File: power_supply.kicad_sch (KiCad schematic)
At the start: 59 parts, among them Q1201 NX7002AK, Q1202 PMN48XP, U1201 TL431AFDT, U1202 TL431AFDT, U1203 TL431AFDT, U1204 MCP1824T-330, U1205 NCV8164ASN120T1G, U1206 MCP1824T-330, U1207 NCV8164ASN250T1G, U1208 NCV8164ASN330T1G

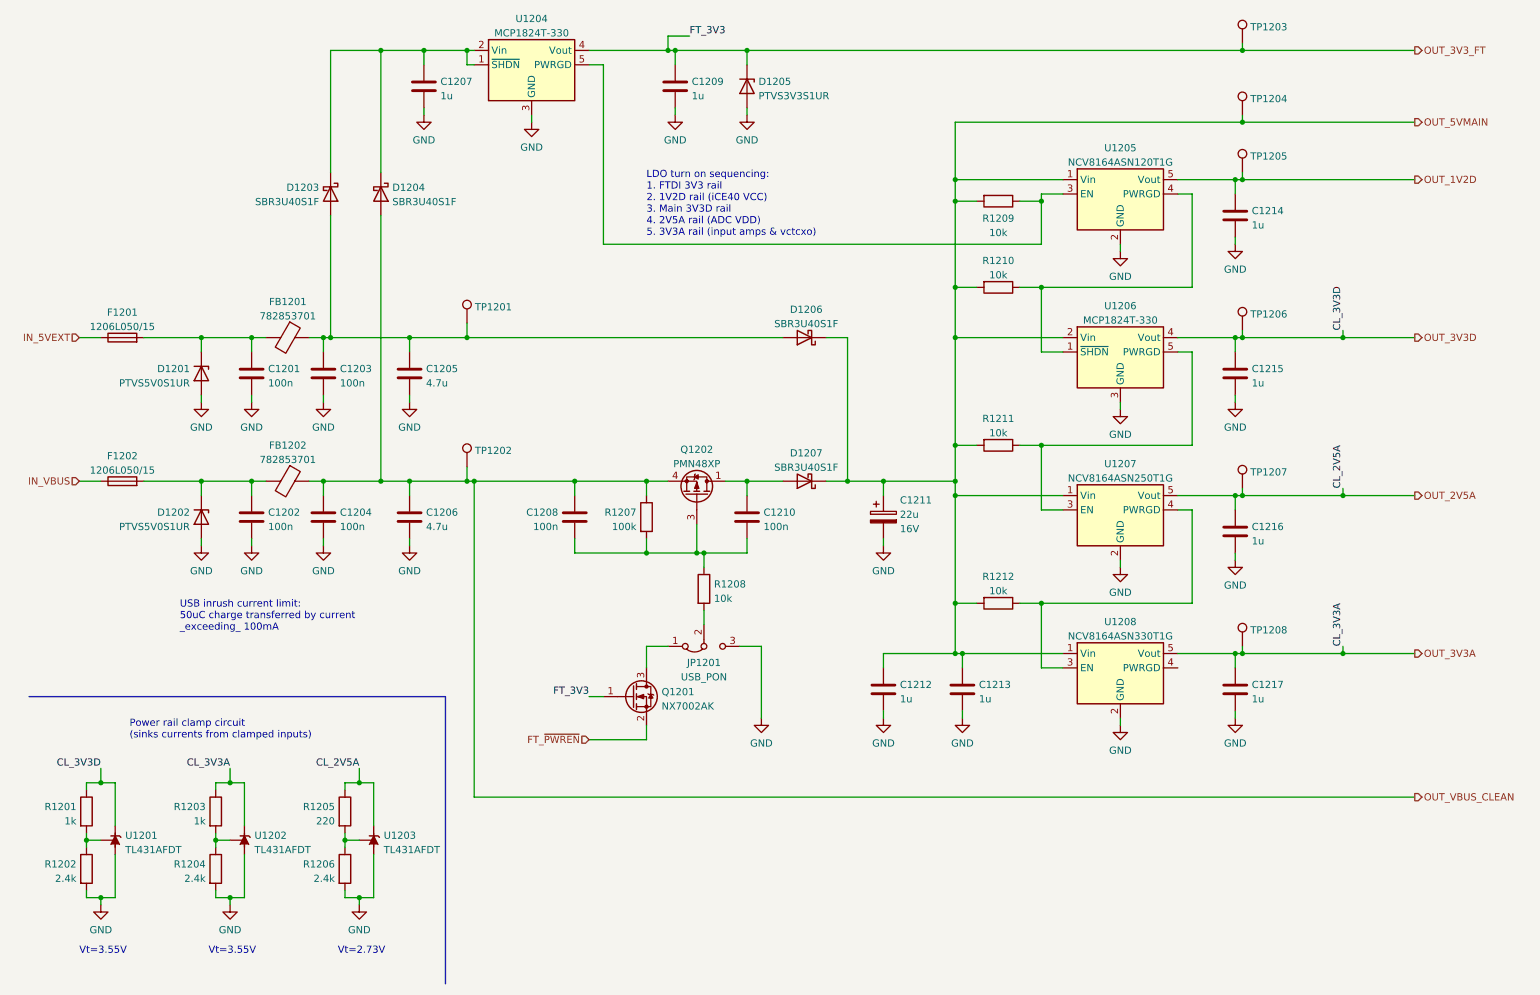
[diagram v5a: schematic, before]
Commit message: Power supply rework - Only fixed power source selection via 0ohm jumpers - Make it simpler
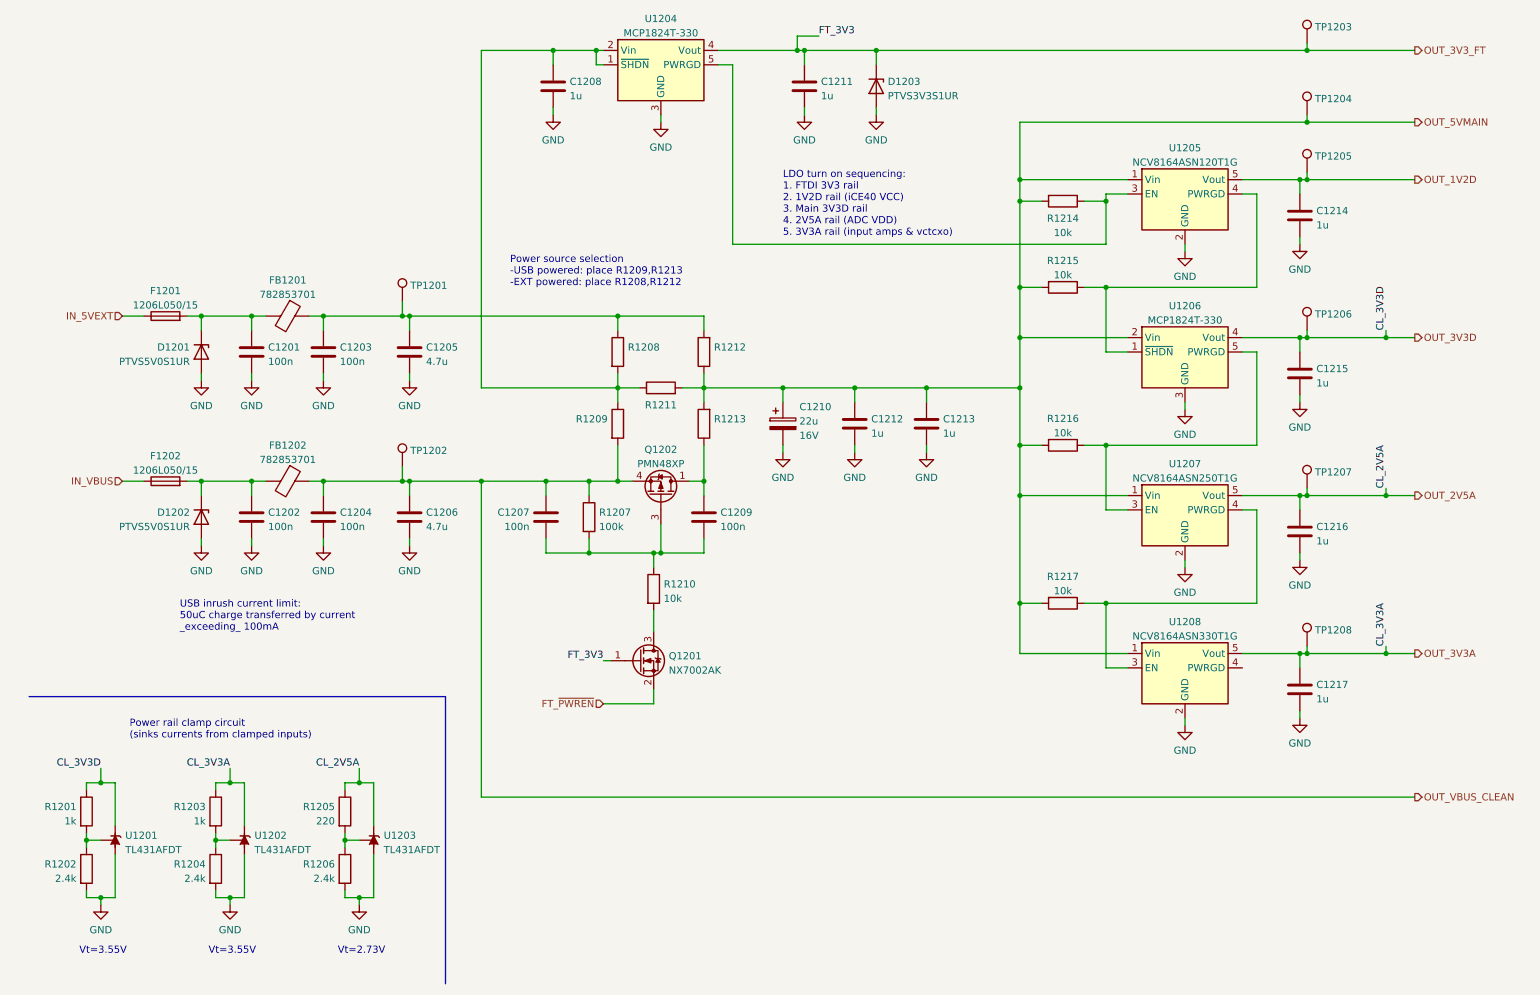
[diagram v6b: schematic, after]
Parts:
- removed D1203, D1204, D1206, D1207: SBR3U40S1F, Diode_SMD:D_SOD-123F, symbol Device:D_Schottky
- removed JP1201: USB_PON, Connector_PinHeader_2.54mm:PinHeader_1x03_P2.54mm_Vertical, symbol Jumper:Jumper_3_Bridged12
- added R1208, R1209, R1211, R1212, R1213: (no value), symbol Device:R
- renumbered C1208 to C1207, C1207 to C1208, C1210 to C1209, C1211 to C1210, C1209 to C1211, D1205 to D1203, R1208 to R1210, R1209 to R1214, R1210 to R1215, R1211 to R1216, R1212 to R1217
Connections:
- net OUT_5VMAIN: now also R1211.2, R1212.1, R1213.2
- net OUT_VBUS_CLEAN: now also R1209.2
- net at C1203.1, C1205.1, FB1201.1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: now also R1208.1, R1212.2
- net at C1209.1, Q1202.1 (D), Q1202.2 (D)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: now also R1213.1
- net at Q1201.3 (D): now also R1210.2
- net at C1208.1, U1204.1 (~{SHDN}), U1204.2 (Vin): now also R1208.2, R1209.1, R1211.1
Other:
- note added: "Power source selection -USB powered: place R1209,R1213 -EXT powered: place R1208,R1212"
- moved on the sheet: C1201, C1203, C1205, C1207, C1208, C1209, C1210, C1211, C1212, C1213, C1214, C1215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

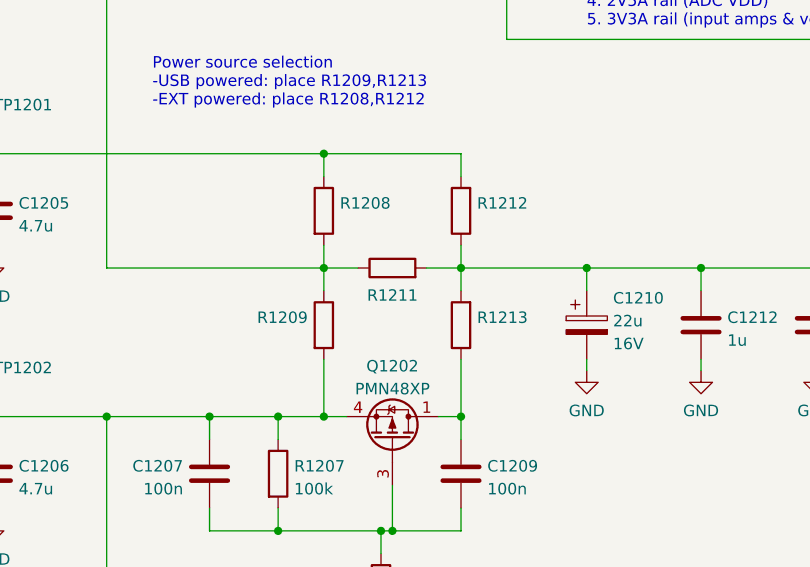
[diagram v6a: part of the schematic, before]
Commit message: Fix footprints, values and PNs
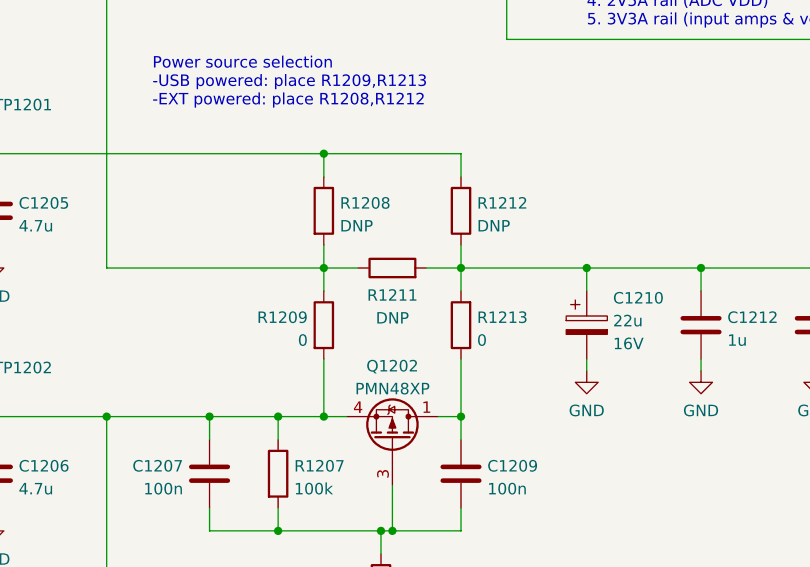
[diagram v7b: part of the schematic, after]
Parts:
- R1208, R1211, R1212: value (none) -> DNP; footprint (none) -> Resistor_SMD:R_0805_2012Metric
- R1209, R1213: value (none) -> 0; footprint (none) -> Resistor_SMD:R_0805_2012Metric; Mfr (none) -> Bourns; Mfr PN (none) -> CR0805-J/-000ELF
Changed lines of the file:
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@@
       (effects (font (size 1.27 1.27)) (justify right))
     )
-    (property "Value" "" (id 1) (at 136.398 80.4422 0)
-      (effects (font (size 1.27 1.27)) (justify right))
-    )
-    (property "Footprint" "" (id 2) (at 136.398 78.74 90)
+    (property "Value" "DNP" (id 1) (at 136.398 80.4422 0)
+      (effects (font (size 1.27 1.27)) (justify right))
+    )
+    (property "Footprint" "Resistor_SMD:R_0805_2012Metric" (id 2) (at 136.398 78.74 90)
       (effects (font (size 1.27 1.27)) hide)
     )
@@
       (effects (font (size 1.27 1.27)) (justify right))
     )
-    (property "Value" "" (id 1) (at 136.398 93.1422 0)
-      (effects (font (size 1.27 1.27)) (justify right))
-    )
-    (property "Footprint" "" (id 2) (at 136.398 91.44 90)
+    (property "Value" "0" (id 1) (at 136.398 93.1422 0)
+      (effects (font (size 1.27 1.27)) (justify right))
+    )
+    (property "Footprint" "Resistor_SMD:R_0805_2012Metric" (id 2) (at 136.398 91.44 90)
       (effects (font (size 1.27 1.27)) hide)
     )
     (property "Datasheet" "~" (id 3) (at 134.62 91.44 0)
+      (effects (font (size 1.27 1.27)) hide)
+    )
+    (property "Mfr" "Bourns" (id 4) (at 134.62 91.44 0)
+      (effects (font (size 1.27 1.27)) hide)
+    )
+    (property "Mfr PN" "CR0805-J/-000ELF" (id 5) (at 134.62 91.44 0)
       (effects (font (size 1.27 1.27)) hide)
     )
@@
       (effects (font (size 1.27 1.27)) (justify left))
     )
-    (property "Value" "" (id 1) (at 121.158 80.4422 0)
-      (effects (font (size 1.27 1.27)) (justify left))
-    )
-    (property "Footprint" "" (id 2) (at 117.602 78.74 90)
+    (property "Value" "DNP" (id 1) (at 121.158 80.4422 0)
+      (effects (font (size 1.27 1.27)) (justify left))
+    )
+    (property "Footprint" "Resistor_SMD:R_0805_2012Metric" (id 2) (at 117.602 78.74 90)
       (effects (font (size 1.27 1.27)) hide)
     )
@@
       (effects (font (size 1.27 1.27)) (justify right))
     )
-    (property "Value" "" (id 1) (at 117.6021 93.1422 0)
-      (effects (font (size 1.27 1.27)) (justify right))
-    )
-    (property "Footprint" "" (id 2) (at 117.602 91.44 90)
+    (property "Value" "0" (id 1) (at 117.6021 93.1422 0)
+      (effects (font (size 1.27 1.27)) (justify right))
+    )
+    (property "Footprint" "Resistor_SMD:R_0805_2012Metric" (id 2) (at 117.602 91.44 90)
       (effects (font (size 1.27 1.27)) hide)
     )
     (property "Datasheet" "~" (id 3) (at 119.38 91.44 0)
+      (effects (font (size 1.27 1.27)) hide)
+    )
+    (property "Mfr" "Bourns" (id 4) (at 119.38 91.44 0)
+      (effects (font (size 1.27 1.27)) hide)
+    )
+    (property "Mfr PN" "CR0805-J/-000ELF" (id 5) (at 119.38 91.44 0)
       (effects (font (size 1.27 1.27)) hide)
     )
@@
     (in_bom yes) (on_board yes) (fields_autoplaced)
     (property "Reference" "R1211" (id 0) (at 127 88.1364 90))
-    (property "Value" "" (id 1) (at 127 90.6733 90))
-    (property "Footprint" "" (id 2) (at 127 86.868 90)
-      (effects (font (size 1.27 1.27)) hide)
-    )
+    (property "Value" "DNP" (id 1) (at 127 90.6733 90))
+    (property "Footprint" "Resistor_SMD:R_0805_2012Metric" (id 2) (at 127 86.868 90)
+      (effects (font (size 1.27 1.27)) hide)
+    )

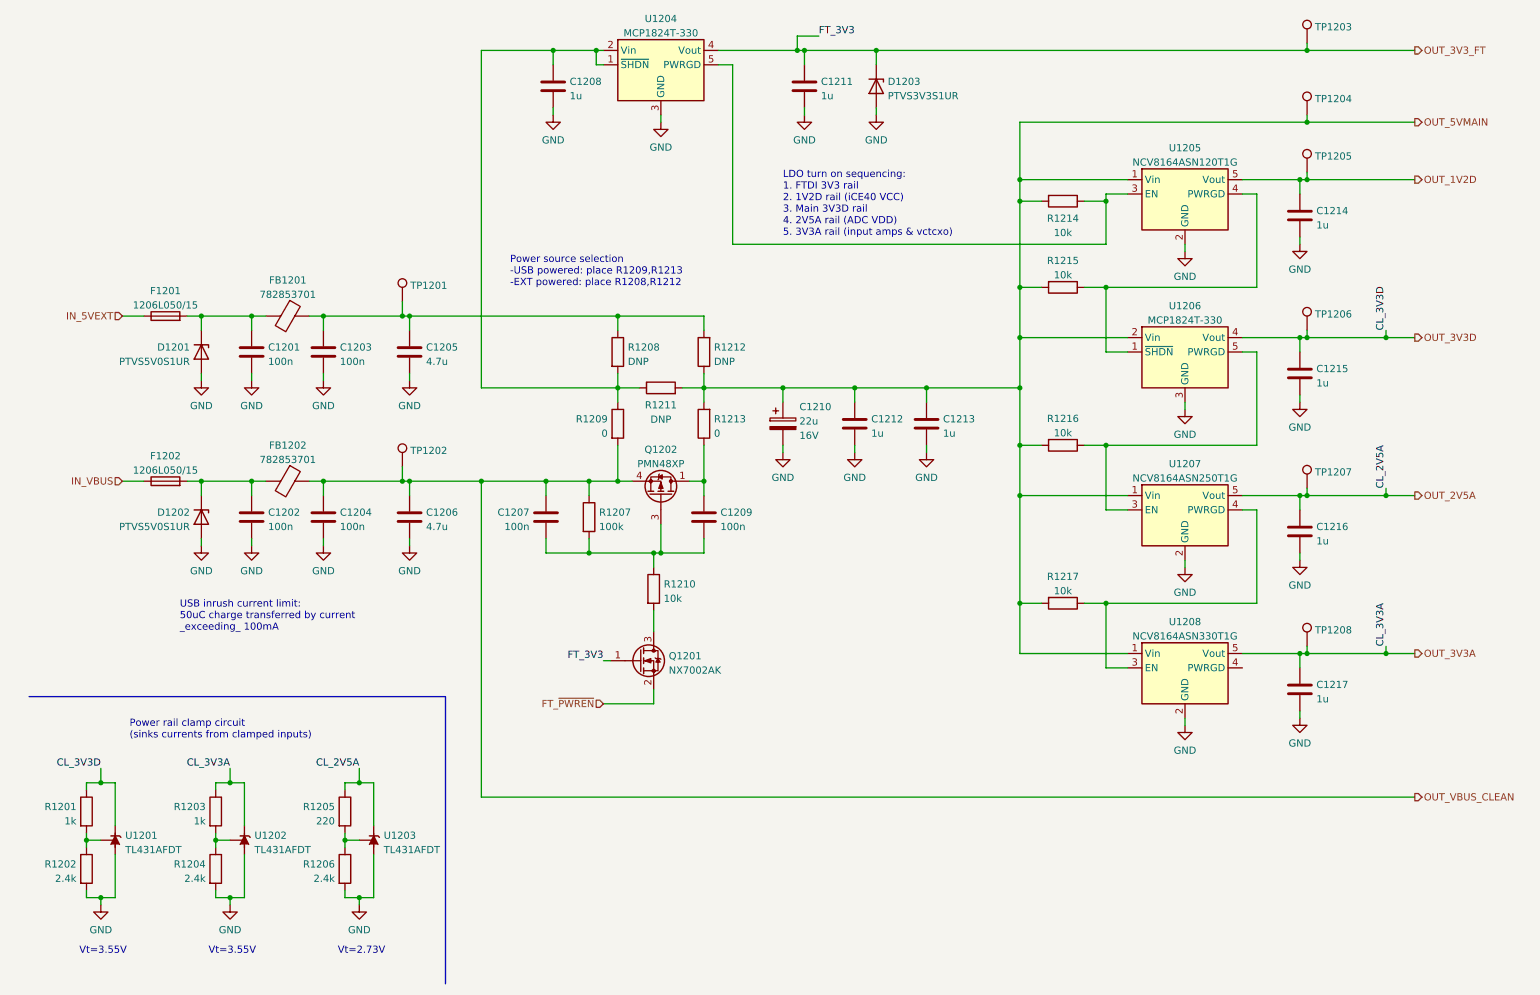
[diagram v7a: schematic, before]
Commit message: Power supply: add +5VFTDI net, prettify net names
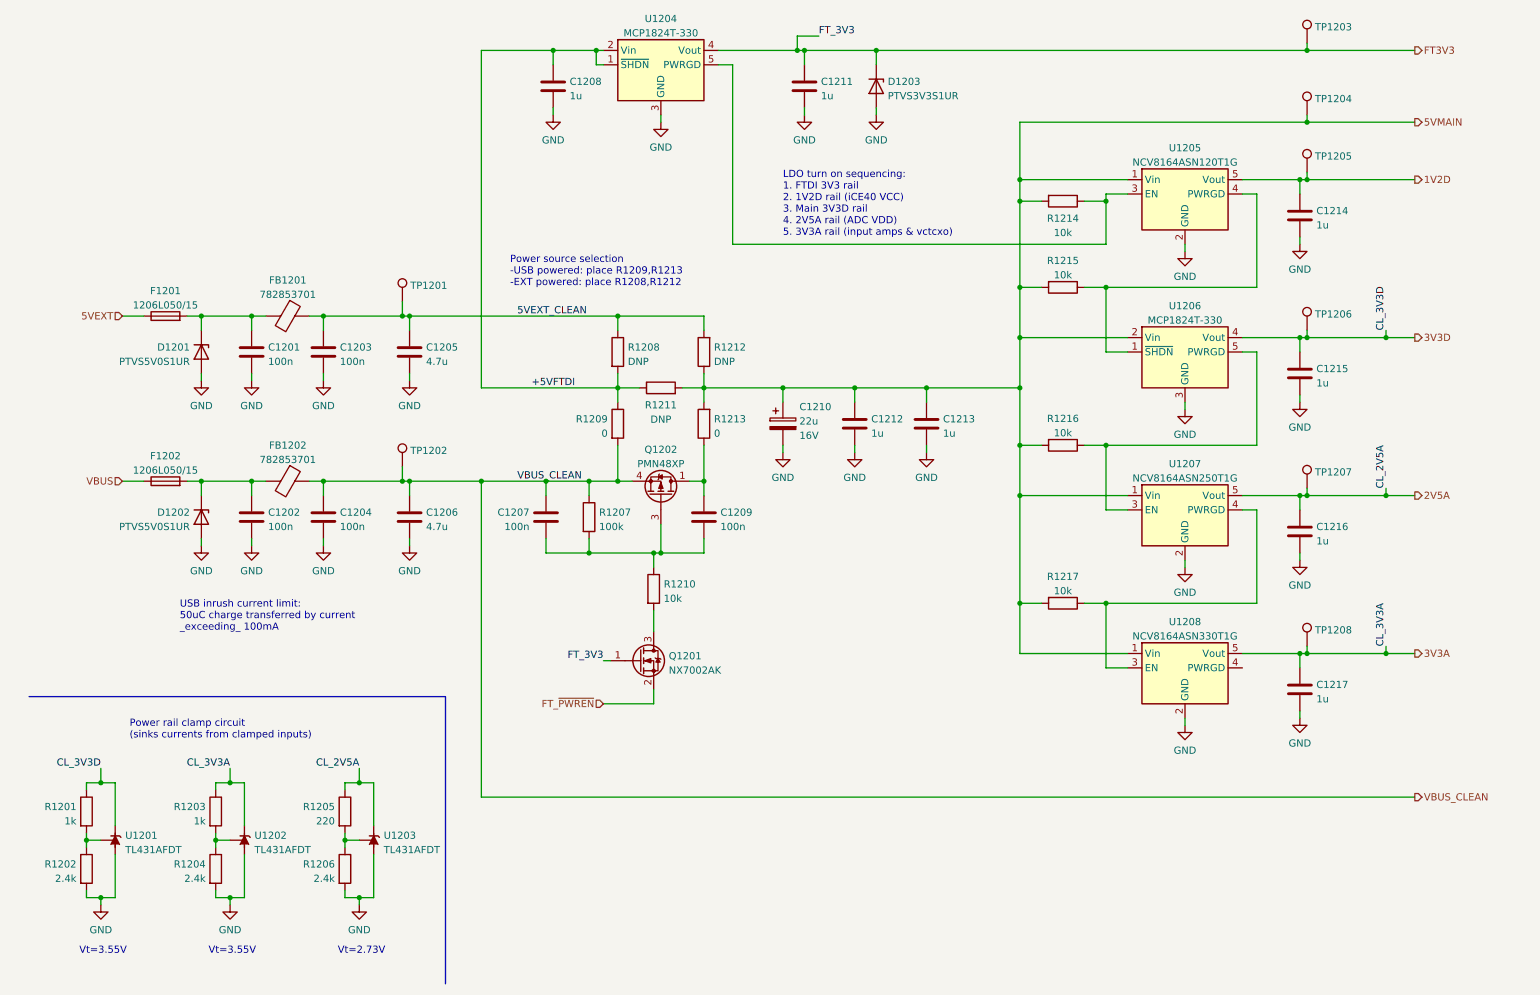
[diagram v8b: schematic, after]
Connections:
- net 5VEXT_CLEAN: now reaches C1203.1, C1205.1, FB1201.1, R1208.1, R1212.2, TP1201.1
- net +5VFTDI: now reaches C1208.1, R1208.2, R1209.1, R1211.1, U1204.1 (~{SHDN}), U1204.2 (Vin)
- net IN_5VEXT renamed 5VEXT
- net IN_VBUS renamed VBUS
- net OUT_1V2D renamed 1V2D
- net OUT_2V5A renamed 2V5A
- net OUT_3V3A renamed 3V3A
- net OUT_3V3D renamed 3V3D
- net OUT_3V3_FT renamed FT3V3
- net OUT_5VMAIN renamed 5VMAIN
- net OUT_VBUS_CLEAN renamed VBUS_CLEAN
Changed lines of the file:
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@@
     (effects (font (size 1.27 1.27)) (justify right bottom))
+  )
+  (label "VBUS_CLEAN" (at 101.6 101.6 0)
+    (effects (font (size 1.27 1.27)) (justify left bottom))
   )
   (label "CL_3V3A" (at 255.27 130.81 90)
@@
   (label "CL_2V5A" (at 73.66 152.4 180)
     (effects (font (size 1.27 1.27)) (justify right bottom))
+  )
+  (label "5VEXT_CLEAN" (at 101.6 72.39 0)
+    (effects (font (size 1.27 1.27)) (justify left bottom))
+  )
+  (label "+5VFTDI" (at 104.14 85.09 0)
+    (effects (font (size 1.27 1.27)) (justify left bottom))
   )
   (label "CL_3V3D" (at 27.94 152.4 180)
@@
     (effects (font (size 1.27 1.27)) (justify left bottom))
   )
-  (hierarchical_label "IN_VBUS" (shape input) (at 31.75 101.6 180)
+  (hierarchical_label "VBUS" (shape input) (at 31.75 101.6 180)
     (effects (font (size 1.27 1.27)) (justify right))
   )
-  (hierarchical_label "OUT_3V3D" (shape output) (at 260.35 76.2 0)
+  (hierarchical_label "3V3D" (shape output) (at 260.35 76.2 0)
     (effects (font (size 1.27 1.27)) (justify left))
   )
-  (hierarchical_label "OUT_1V2D" (shape output) (at 260.35 48.26 0)
+  (hierarchical_label "1V2D" (shape output) (at 260.35 48.26 0)
     (effects (font (size 1.27 1.27)) (justify left))
   )
-  (hierarchical_label "IN_5VEXT" (shape input) (at 31.75 72.39 180)
+  (hierarchical_label "5VEXT" (shape input) (at 31.75 72.39 180)
     (effects (font (size 1.27 1.27)) (justify right))
   )
-  (hierarchical_label "OUT_3V3_FT" (shape output) (at 260.35 25.4 0)
+  (hierarchical_label "FT3V3" (shape output) (at 260.35 25.4 0)
     (effects (font (size 1.27 1.27)) (justify left))
   )
-  (hierarchical_label "OUT_5VMAIN" (shape output) (at 260.35 38.1 0)
+  (hierarchical_label "5VMAIN" (shape output) (at 260.35 38.1 0)
     (effects (font (size 1.27 1.27)) (justify left))
   )
-  (hierarchical_label "OUT_VBUS_CLEAN" (shape output) (at 260.35 157.48 0)
+  (hierarchical_label "VBUS_CLEAN" (shape output) (at 260.35 157.48 0)
     (effects (font (size 1.27 1.27)) (justify left))
   )
@@
     (effects (font (size 1.27 1.27)) (justify right))
   )
-  (hierarchical_label "OUT_3V3A" (shape output) (at 260.35 132.08 0)
+  (hierarchical_label "3V3A" (shape output) (at 260.35 132.08 0)
     (effects (font (size 1.27 1.27)) (justify left))
   )
-  (hierarchical_label "OUT_2V5A" (shape output) (at 260.35 104.14 0)
+  (hierarchical_label "2V5A" (shape output) (at 260.35 104.14 0)
     (effects (font (size 1.27 1.27)) (justify left))
   )
